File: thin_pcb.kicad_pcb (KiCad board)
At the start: 2 copper layers, 95.2 x 95.2 mm, 191 parts, among them J01 Conn_01x02, J02 Conn_01x02, J04 Conn_01x02, J06 Conn_01x02, J07 Conn_01x02, J08 Conn_01x02, J1 USB_B_Micro, J11 Conn_01x03, J12 Conn_01x03, J13 Conn_01x03, J14 Conn_01x03, J15 Conn_01x03, J16 Conn_01x03, J17 Conn_01x03, J18 Conn_01x03, J2 AudioJack4_Ground, J21 Conn_01x07, J22 Conn_01x07, J23 Conn_01x07, J24 Conn_01x07, J25 Conn_01x07, J26 Conn_01x07, J27 Conn_01x07, J28 Conn_01x07, J3 AudioJack4_Ground, J31 Conn_01x07, J32 Conn_01x07, J33 Conn_01x07, J34 Conn_01x07, J35 Conn_01x07, J36 Conn_01x07, J37 Conn_01x07, J38 Conn_01x07, J4 Conn_01x06, J41 Conn_01x04, J42 Conn_01x04, J43 Conn_01x04, J44 Conn_01x04, J45 Conn_01x04, J46 Conn_01x04, J47 Conn_01x04, J48 Conn_01x04, J5 Conn_01x06, J51 Conn_01x01, J52 Conn_01x01, J53 Conn_01x01, J54 Conn_01x01, J55 Conn_01x01, J56 Conn_01x01, J57 Conn_01x01, J58 Conn_01x01, J6 Conn_02x02, J7 Conn_01x02, SW11 SW_Push, SW12 SW_Push, SW13 SW_Push, SW14 SW_Push, SW15 SW_Push, SW21 SW_Push, SW22 SW_Push, SW23 SW_Push, SW24 SW_Push, SW25 SW_Push, SW252 SW_Push, SW31 SW_Push, SW32 SW_Push, SW33 SW_Push, SW34 SW_Push, SW35 SW_Push, SW41 SW_Push, SW42 SW_Push, SW422 SW_Push, SW43 SW_Push, SW44 SW_Push, SW45 SW_Push, SW452 SW_Push, SW51 SW_Push, SW52 SW_Push, SW522 SW_Push, SW53 SW_Push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

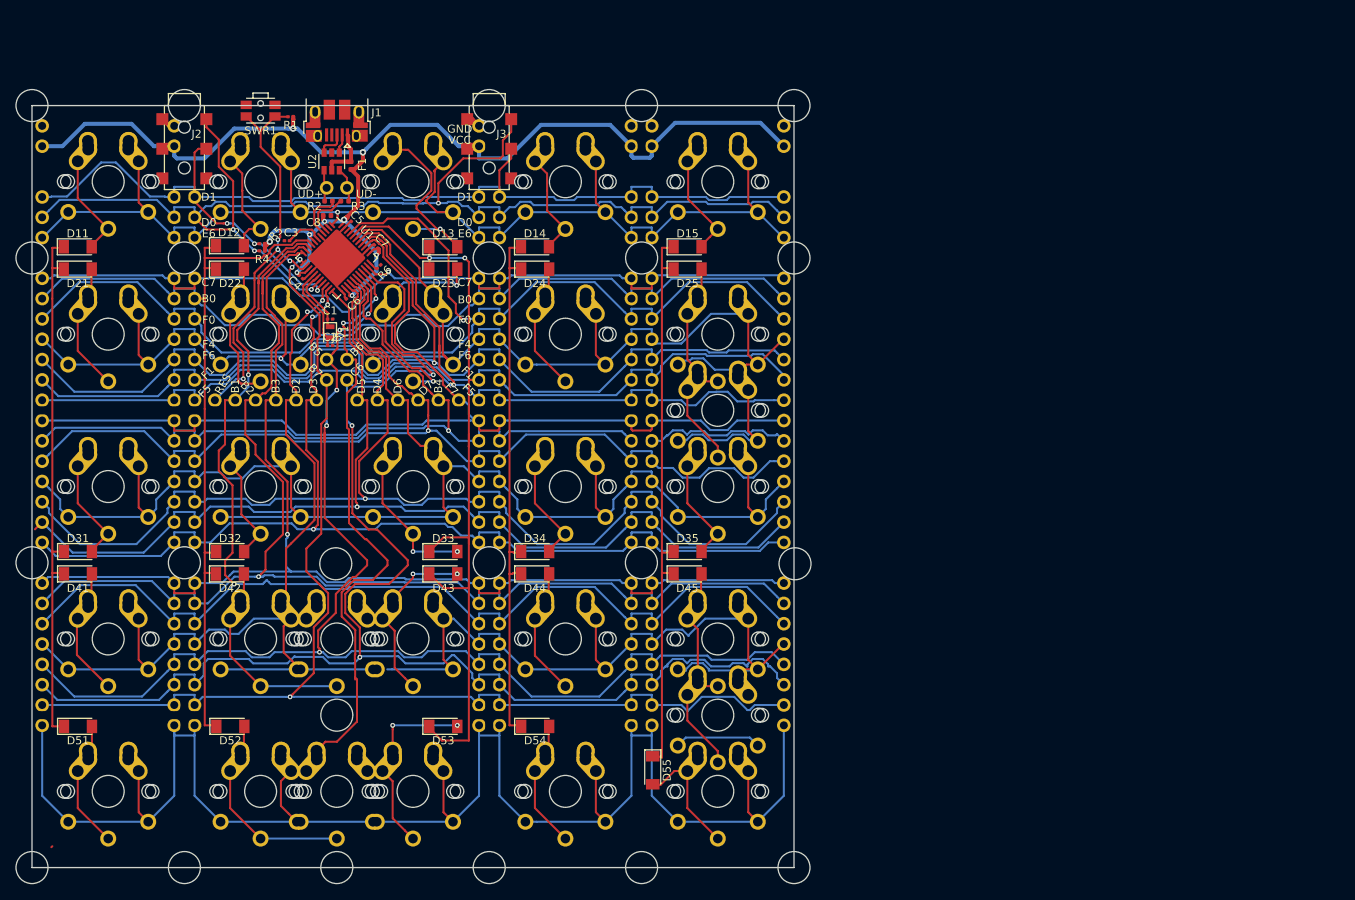
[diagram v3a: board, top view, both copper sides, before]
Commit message: smd 0603->1005 & fixes
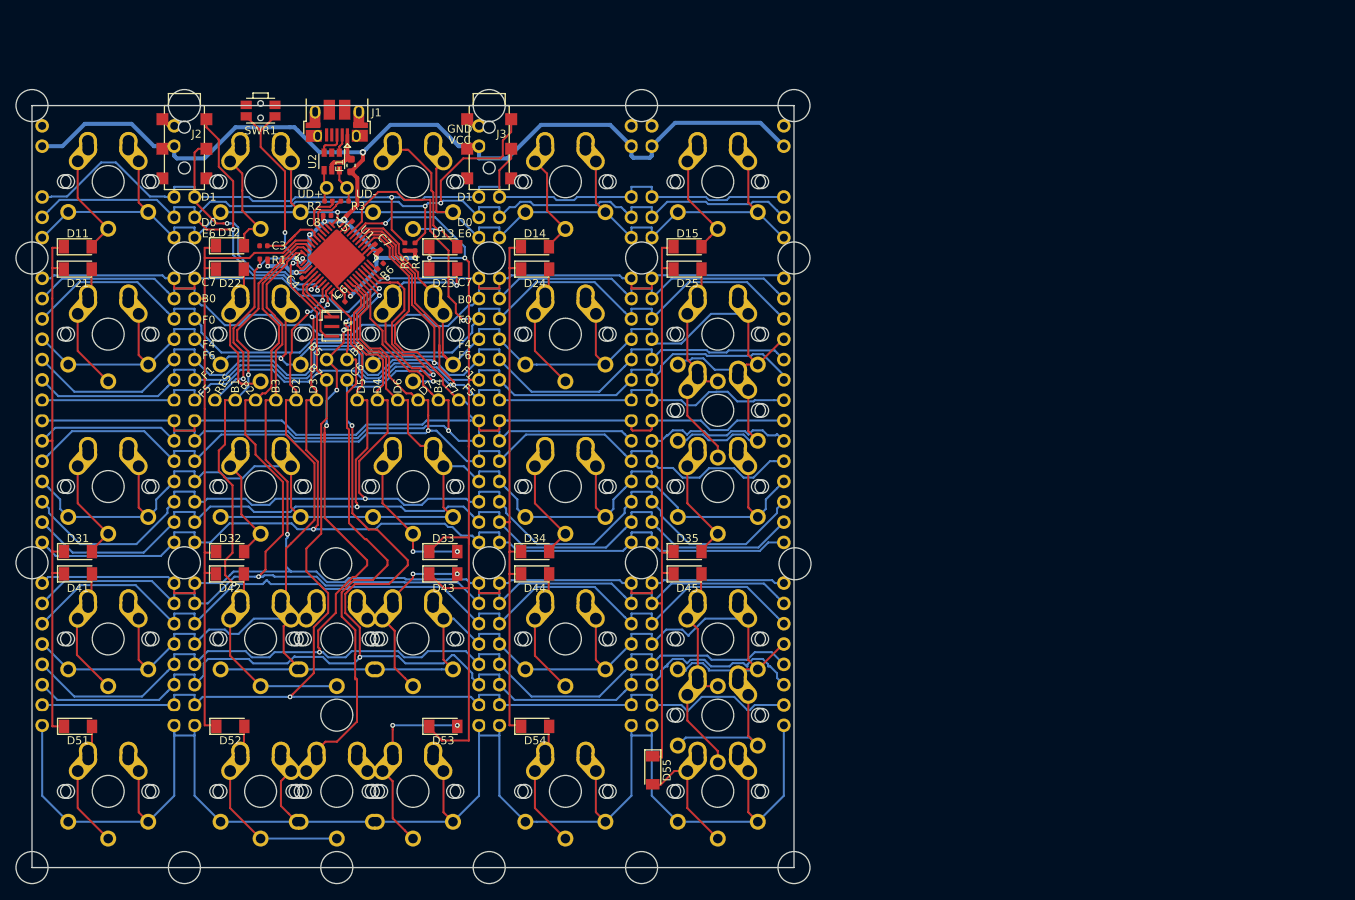
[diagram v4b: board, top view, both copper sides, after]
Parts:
- removed the ? at (105.4, 81.9) (x2)
- removed C1, C2: 22p, Capacitor_SMD:C_0201_0603Metric
- added ? (x2): , , F.Cu at (105.4, 81.9)
- C3, C4, C5, C6, C7: footprint Capacitor_SMD:C_0201_0603Metric -> Capacitor_SMD:C_0402_1005Metric
- F1: footprint Fuse:Fuse_0402_1005Metric -> Fuse:Fuse_0603_1608Metric
- R1, R4, R5, R6: footprint Resistor_SMD:R_0201_0603Metric -> Resistor_SMD:R_0402_1005Metric
- Y1: footprint Crystal:Crystal_SMD_2012-2Pin_2.0x1.2mm -> Crystal:Resonator_SMD_muRata_CSTxExxV-3Pin_3.0x1.1mm
- moved R4 19.1 mm to (99.3, 76.7), turned to 90 degrees
- moved R1 18.1 mm to (80.4, 78.2)
- moved R5 17.8 mm to (98.0, 76.7), turned to 90 degrees
- moved C3 3.01 mm to (80.4, 76.6)
- moved Y1 0.76 mm to (88.9, 86.7)
- moved C4 0.29 mm to (84.8, 80.3)
- moved C6 0.22 mm to (90.9, 83.2)
- moved C7 0.22 mm to (94.7, 76.7)
- moved R6 0.22 mm to (95.0, 79.1)
- moved C5 0.11 mm to (91.1, 73.2)
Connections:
- J7 pad 1: UD+ -> CD+
- J7 pad 2: UD- -> CD-
- R2 pad 2: UD+ -> CD+
- R3 pad 1: UD- -> CD-
- U2 pad 4: UD+ -> CD+
- U2 pad 6: UD- -> CD-
- Y1 pad 2: XTAL2 -> GND
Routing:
- net D2: track 225.2 -> 236.2 mm
- net D1: track 141.8 -> 149.6 mm
- net F1: track 216.4 -> 222.6 mm, vias 2 -> 3
- net F0: track 144.1 -> 150.1 mm
- net D0: track 161.7 -> 167.6 mm
- net UD-: track 6.84 -> 2.36 mm
- net CD-: track 0.00 -> 4.33 mm
- net UD+: track 7.84 -> 3.62 mm
- net CD+: track 0.00 -> 4.12 mm
- net Net-(C3-Pad1): track 4.83 -> 8.77 mm
- net VCC: track 168.0 -> 169.7 mm
- net B6: track 284.9 -> 286.5 mm
- net Net-(D13-Pad2): track 21.9 -> 20.4 mm
- net XTAL1: track 8.08 -> 6.93 mm
- net E6: track 150.0 -> 148.8 mm
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
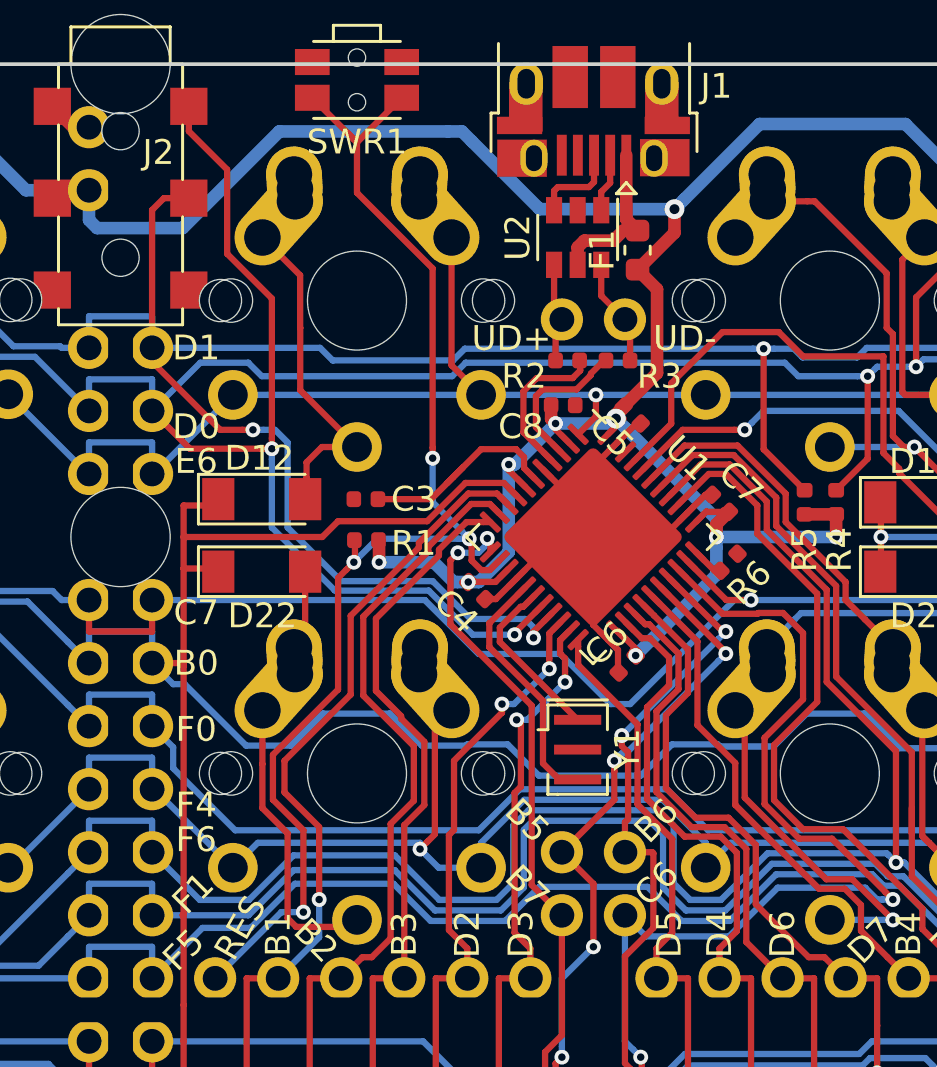
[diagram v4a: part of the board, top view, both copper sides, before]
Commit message: aref cond & positioning
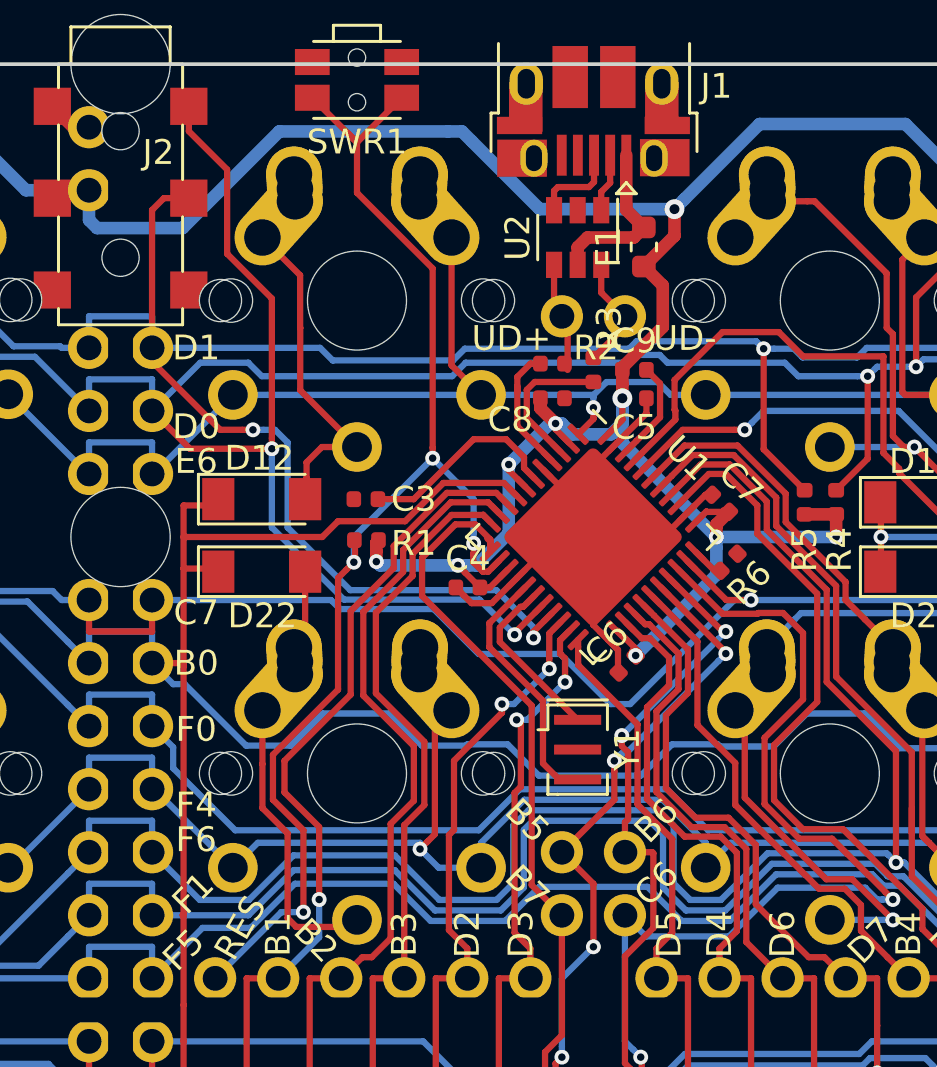
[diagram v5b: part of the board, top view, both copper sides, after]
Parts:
- removed the ? at (105.4, 81.9) (x2)
- added ? (x2): , , F.Cu at (105.4, 81.9)
- added C9: 0.1u, Capacitor_SMD:C_0402_1005Metric, F.Cu at (91.2, 71.4)
- moved R3 1.06 mm to (89.5, 71.4), turned to 270 degrees
- moved C5 0.68 mm to (91.2, 72.5), turned to 180 degrees
- moved R2 0.63 mm to (87.9, 71.1), turned to 0 degrees
- moved C8 0.51 mm to (87.9, 72.5)
- moved C4 0.38 mm to (84.5, 80.1), turned to 0 degrees
- moved F1 0.28 mm to (91.6, 66.4)
- moved J7 0.13 mm to (88.3, 69.2)
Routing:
- net Net-(C9-Pad2): track 0.00 -> 4.11 mm
- net B7: track 165.7 -> 168.4 mm, vias 3 -> 1
- net GND: track 32.5 -> 35.1 mm
- net VCC: track 169.7 -> 172.2 mm
- net D+: track 6.18 -> 5.34 mm
- net B3: track 149.3 -> 150.1 mm
- net CD+: track 4.12 -> 4.82 mm
- net B2: track 232.9 -> 233.5 mm
- net Net-(C3-Pad1): track 8.77 -> 8.21 mm
- net B1: track 168.5 -> 169.0 mm
- net RESET: track 52.2 -> 52.8 mm

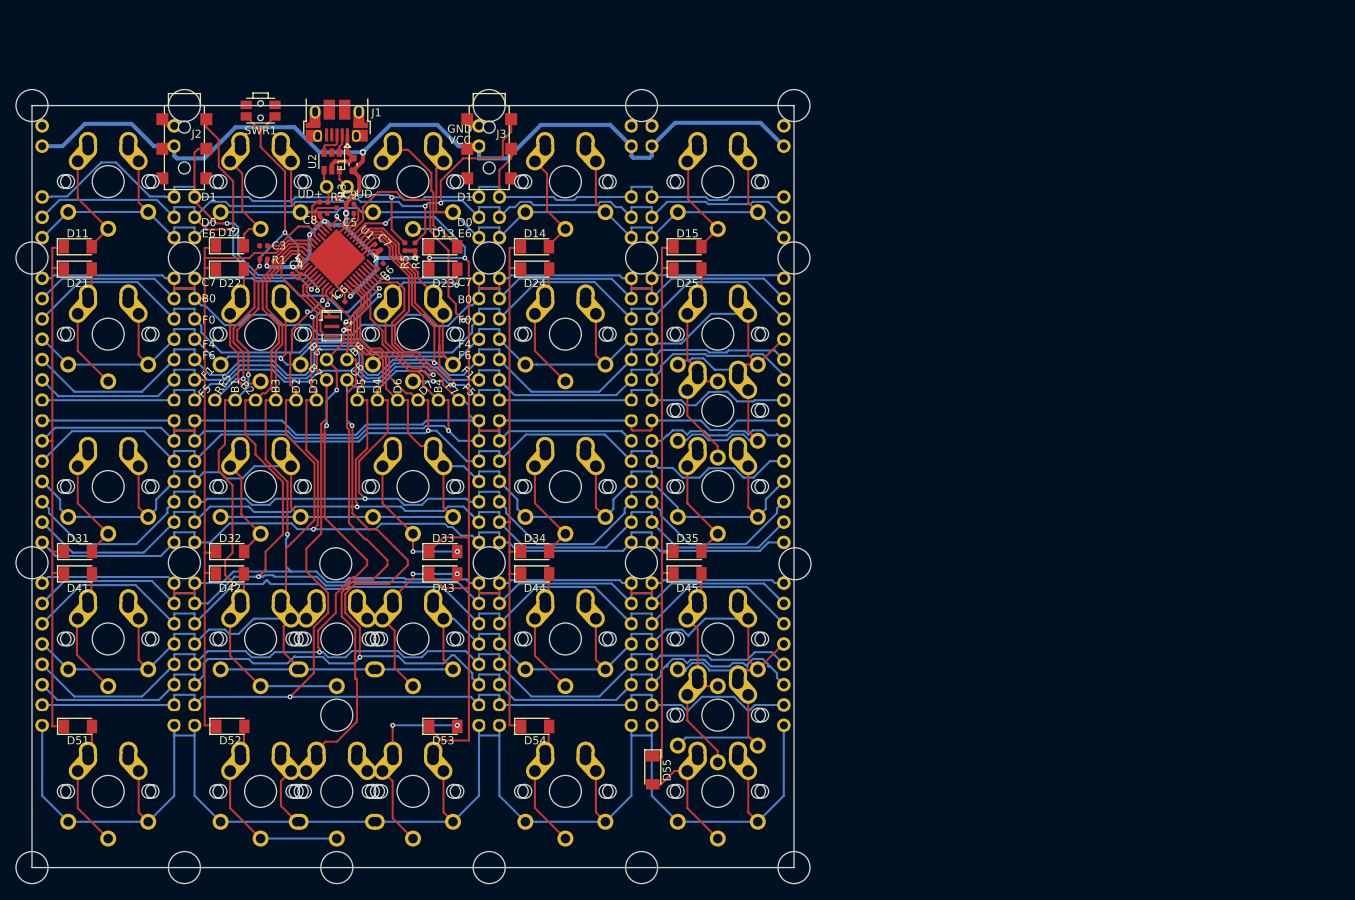
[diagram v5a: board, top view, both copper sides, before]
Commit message: some traces aligning
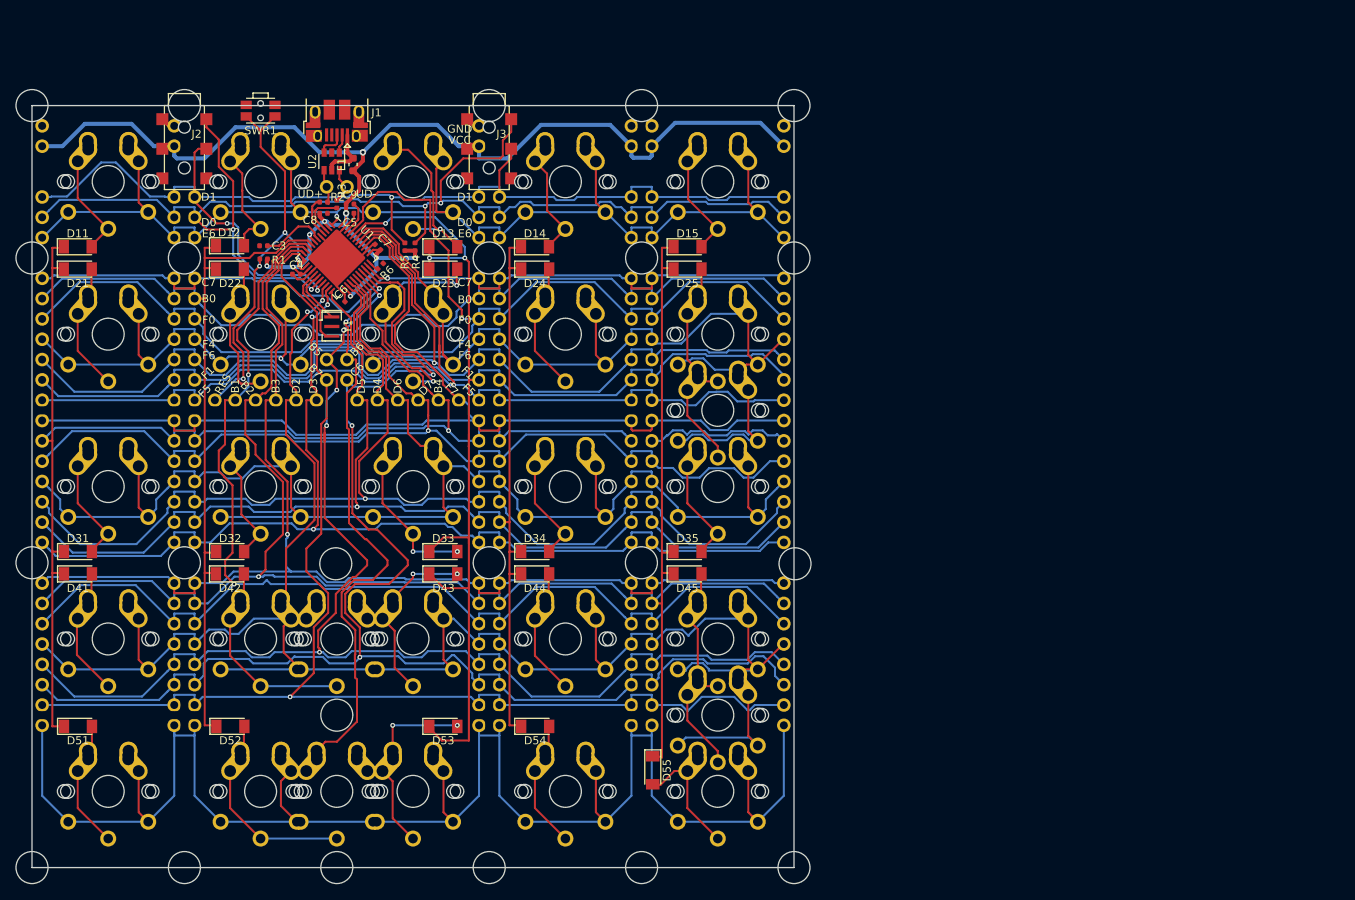
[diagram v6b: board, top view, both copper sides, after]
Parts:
- removed the ? at (105.4, 81.9) (x2)
- added ? (x2): , , F.Cu at (105.4, 81.9)
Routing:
- net C6: track 192.4 -> 191.5 mm

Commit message: fixes
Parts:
- removed the ? at (105.4, 81.9) (x2)
- added ? (x2): , , F.Cu at (105.4, 81.9)
- moved C4 0.13 mm to (84.4, 80.1)
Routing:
- net B4: track 198.4 -> 200.8 mm
- net GND: track 35.1 -> 32.9 mm
